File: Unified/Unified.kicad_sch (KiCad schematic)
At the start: 15 parts, among them J1 Conn_Coaxial_Power, J2 Screw_Terminal_01x02, J3 Screw_Terminal_01x02, J4 Conn_01x04_Male, J5 Screw_Terminal_01x04, Q1 IRLB8721PBF, Q2 IRLB8721PBF, Q3 IRLB8721PBF, Q4 IRLB8721PBF, SW1 SW_SPST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

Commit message: Removes 12V and Ground outputs to LED strip. This will be done with thicker wire outside of PCB, due to high trace width requirements
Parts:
- removed C1: 1000uF, Capacitor_THT:CP_Radial_D5.0mm_P2.00mm, symbol Device:C
- removed J1: Conn_Coaxial_Power, Connector_BarrelJack:BarrelJack_Horizontal, symbol Connector:Conn_Coaxial_Power
- removed J3: Screw_Terminal_01x02, TerminalBlock:TerminalBlock_bornier-2_P5.08mm, symbol Connector:Screw_Terminal_01x02
- added J1: Screw_Terminal_01x02, TerminalBlock:TerminalBlock_bornier-2_P5.08mm, symbol Connector:Screw_Terminal_01x02
- added U3: TSOP382xx, OptoDevice:Vishay_MINICAST-3Pin, symbol Interface_Optical:TSOP382xx
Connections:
- net +12V: now also J1.2 (Pin_2)
- net +5V: now also U3.3 (Vs)
- net GND: now also J1.1 (Pin_1), U3.2 (GND)
- net at U1.20 (IO4): now also U3.1 (OUT)
- no-connect marks 21 -> 20

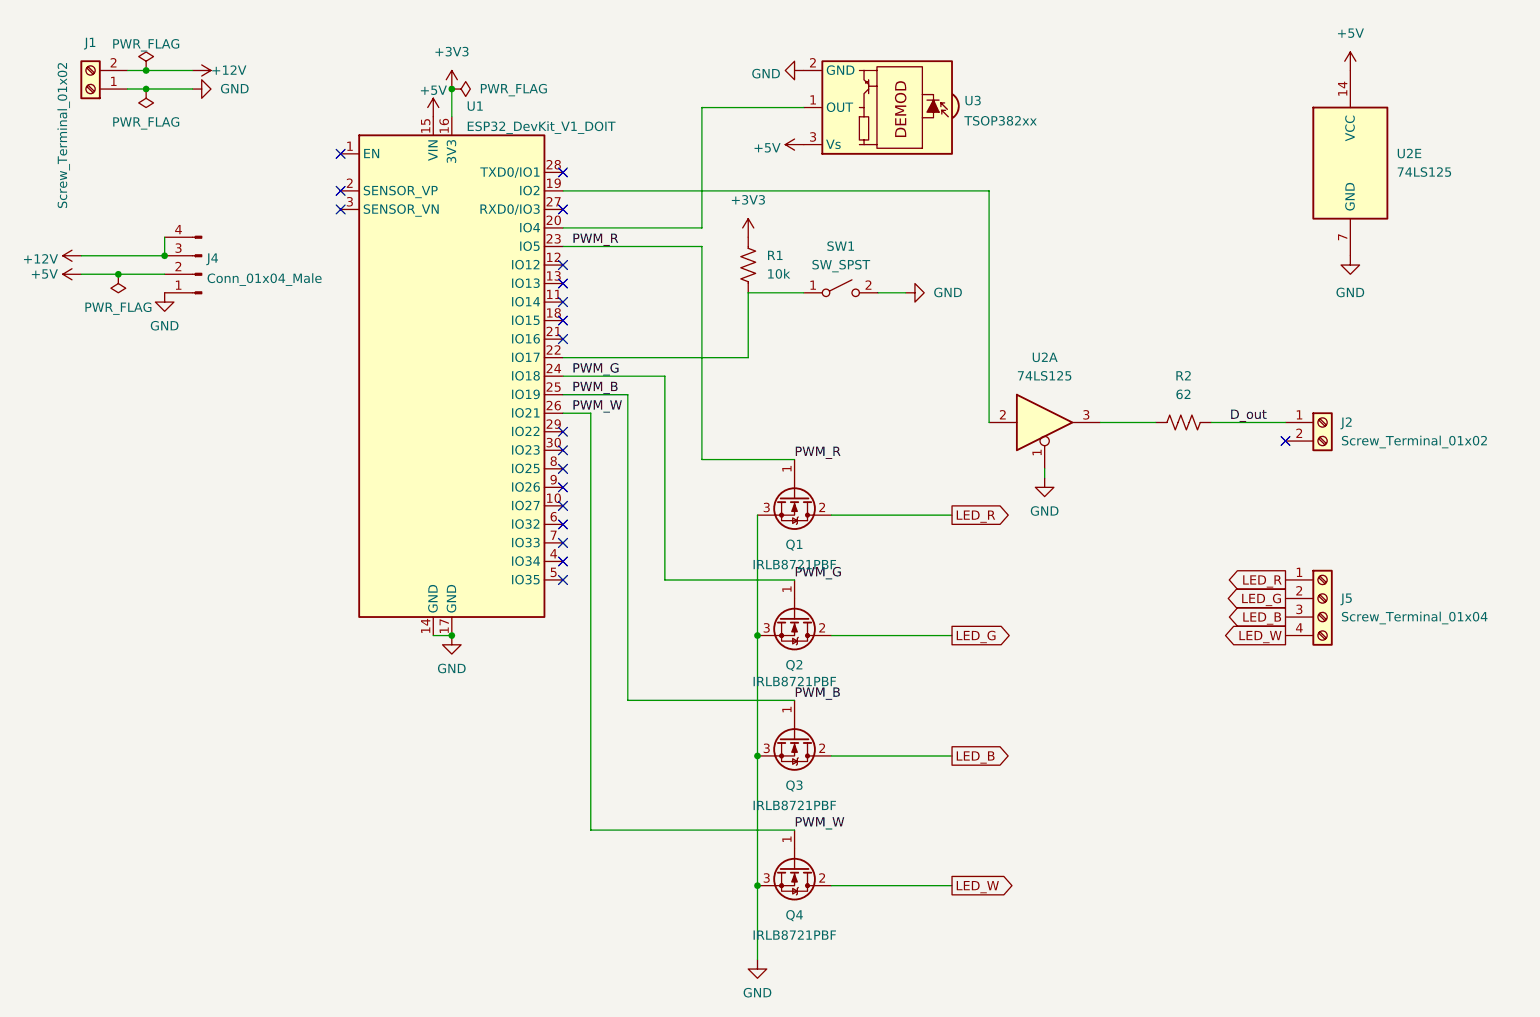
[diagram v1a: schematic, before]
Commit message: Adds custom symbol for the level shifter
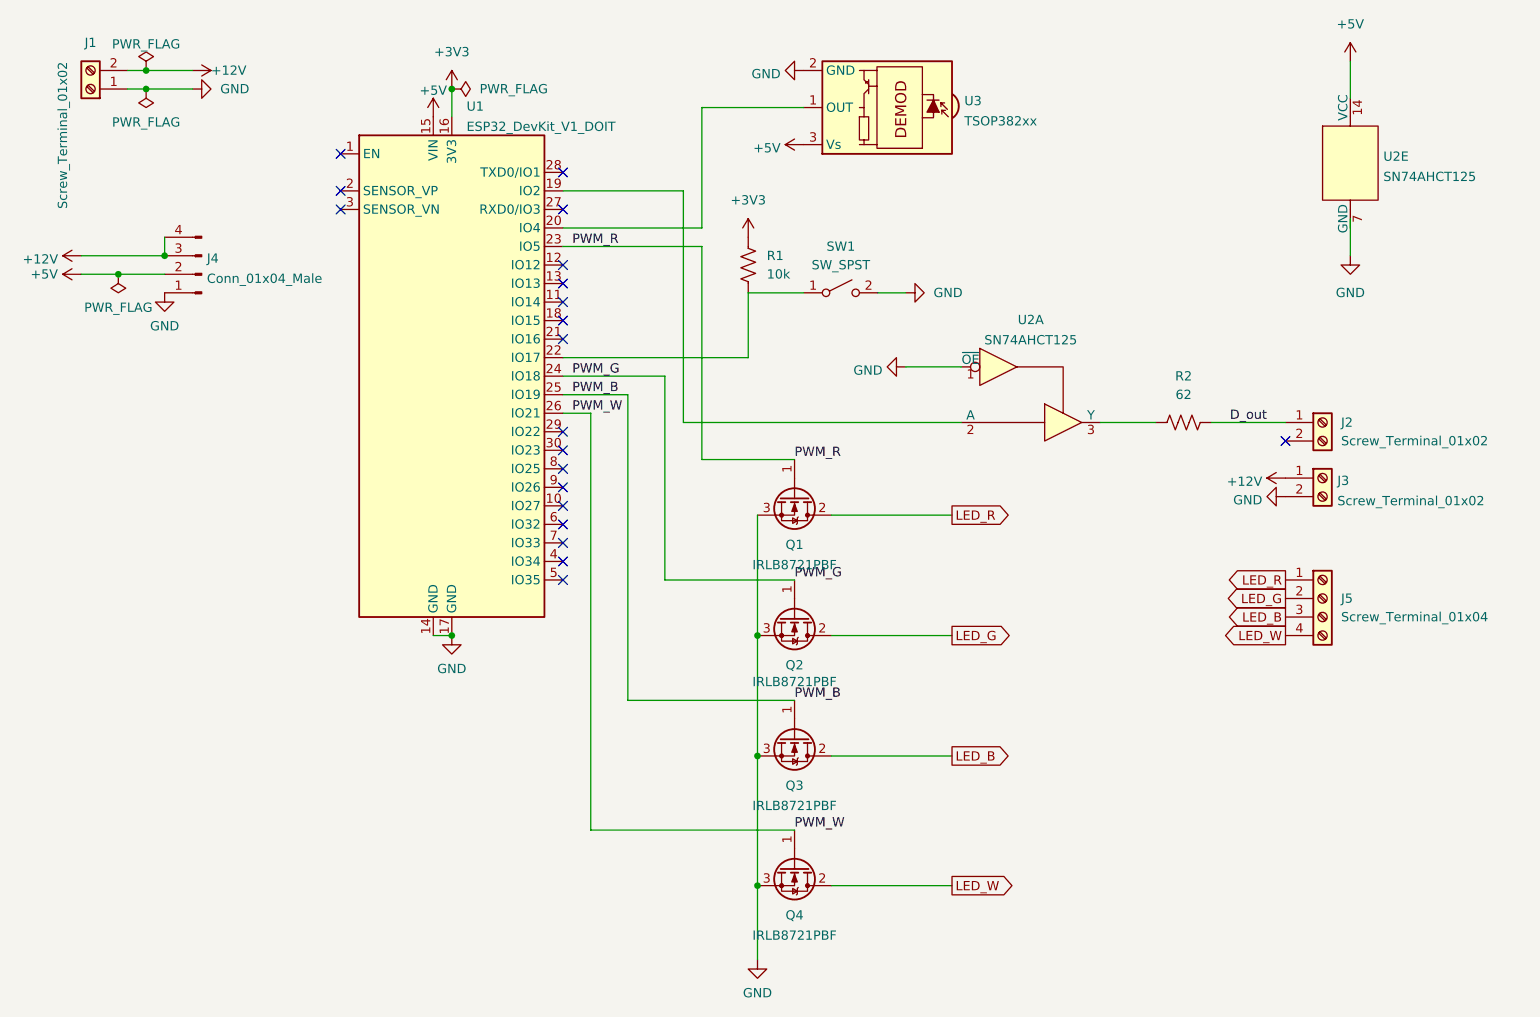
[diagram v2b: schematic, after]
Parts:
- removed U2: 74LS125, Package_DIP:DIP-14_W7.62mm, symbol 74xx:74LS125
- added J3: Screw_Terminal_01x02, TerminalBlock_Dinkle:TerminalBlock_Dinkle_DT-55-B01X-02_P10.00mm, symbol Connector:Screw_Terminal_01x02
- added U2: SN74AHCT125, Package_DIP:DIP-14_W7.62mm, symbol custom_symbols:SN74AHCT125
- J1: footprint TerminalBlock:TerminalBlock_bornier-2_P5.08mm -> TerminalBlock_Dinkle:TerminalBlock_Dinkle_DT-55-B01X-02_P10.00mm
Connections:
- net +12V: now also J3.1 (Pin_1)
- net +5V: now also U2.14 (VCC)
- net GND: now also J3.2 (Pin_2), U2.1 (~{OE})
- net at R2.1: now also U2.3 (Y)
- net at U1.19 (IO2): now also U2.2 (A)
